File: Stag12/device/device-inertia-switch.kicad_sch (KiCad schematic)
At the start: 2 parts

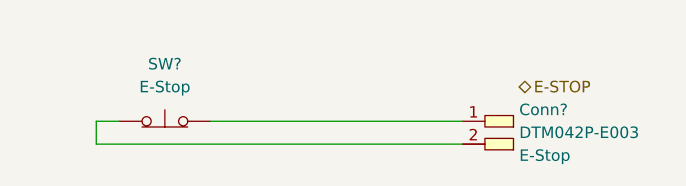
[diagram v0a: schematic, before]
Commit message: Changed filepaths
Makes graphical explorers a bit neater

TODO: Decide on new paths for each device (maybe geographical?)
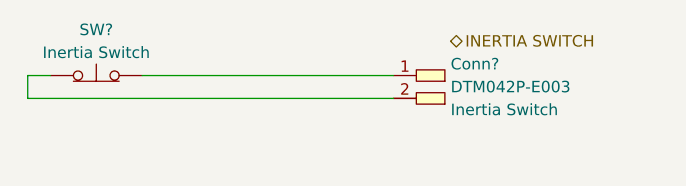
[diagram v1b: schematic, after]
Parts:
- removed Conn?: Deutsch_DTM_2P_Pin, symbol Connectors_SUFST:Deutsch_DTM_2P_Pin
- removed SW?: E-Stop, symbol Switch:SW_Push_Open
- added Conn?: Deutsch_DTM_2P_Pin, symbol Connectors_SUFST:Deutsch_DTM_2P_Pin
- added SW?: Inertia Switch, symbol Switch:SW_Push_Open
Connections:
- new net: Conn?.2, SW?.1 (A)
- new net: Conn?.1, SW?.2 (B)
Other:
- title: DEVICE - E-STOP -> DEVICE - INERTIA SWITCH
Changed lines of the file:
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@@
 	(paper "A4")
 	(title_block
-		(title "DEVICE - E-STOP")
-	)
-	(wire
-		(pts
-			(xy 119.38 99.06) (xy 116.84 99.06)
-		)
-		(stroke
-			(width 0)
-			(type default)
-		)
-	)
-	(wire
-		(pts
-			(xy 116.84 101.6) (xy 157.48 101.6)
-		)
-		(stroke
-			(width 0)
-			(type default)
-		)
-	)
-	(wire
-		(pts
-			(xy 116.84 99.06) (xy 116.84 101.6)
-		)
-		(stroke
-			(width 0)
-			(type default)
-		)
-	)
-	(wire
-		(pts
-			(xy 129.54 99.06) (xy 157.48 99.06)
-		)
-		(stroke
-			(width 0)
-			(type default)
-		)
-	)
-	(hierarchical_label "E-STOP"
+		(title "DEVICE - INERTIA SWITCH")
+	)
+	(wire
+		(pts
+			(xy 109.22 96.52) (xy 149.86 96.52)
+		)
+		(stroke
+			(width 0)
+			(type default)
+		)
+	)
+	(wire
+		(pts
+			(xy 121.92 93.98) (xy 149.86 93.98)
+		)
+		(stroke
+			(width 0)
+			(type default)
+		)
+	)
+	(wire
+		(pts
+			(xy 109.22 93.98) (xy 109.22 96.52)
+		)
+		(stroke
+			(width 0)
+			(type default)
+		)
+	)
+	(wire
+		(pts
+			(xy 111.76 93.98) (xy 109.22 93.98)
+		)
+		(stroke
+			(width 0)
+			(type default)
+		)
+	)
+	(hierarchical_label "INERTIA SWITCH"
 		(shape bidirectional)
-		(at 163.83 95.25 0)
+		(at 156.21 90.17 0)
 		(effects
 			(font
@@
 	(symbol
 		(lib_id "Switch:SW_Push_Open")
-		(at 124.46 99.06 0)
+		(at 116.84 93.98 0)
 		(unit 1)
 		(exclude_from_sim no)
@@
 		(fields_autoplaced yes)
 		(property "Reference" "SW?"
-			(at 124.46 92.71 0)
-			(effects
-				(font
-					(size 1.27 1.27)
-				)
-			)
-		)
-		(property "Value" "E-Stop"
-			(at 124.46 95.25 0)
+			(at 116.84 88.9 0)
+			(effects
+				(font
+					(size 1.27 1.27)
+				)
+			)
+		)
+		(property "Value" "Inertia Switch"
+			(at 116.84 91.44 0)
 			(effects
 				(font
@@
 		)
 		(property "Footprint" ""
-			(at 124.46 93.98 0)
+			(at 116.84 88.9 0)
 			(effects
 				(font
@@
 		)
 		(property "Datasheet" "~"
-			(at 124.46 93.98 0)
+			(at 116.84 88.9 0)
 			(effects
 				(font
@@
 		)
 		(property "Description" ""
-			(at 124.46 99.06 0)
+			(at 116.84 93.98 0)
 			(effects
 				(font
@@
 		)
 		(property "Conn Name" ""
-			(at 124.46 95.25 0)
+			(at 116.84 90.17 0)
 			(effects
 				(font
@@
 		)
 		(instances
-			(project "Stag11"
-				(path "/03011643-0690-4b85-ab78-d6a62dae52b1/3cdef822-b27b-4a71-b67b-74c9f7188311"
+			(project "Stag12"
+				(path "/03011643-0690-4b85-ab78-d6a62dae52b1/f29d1e22-db5a-4e21-943f-a4075fd10598"
 					(reference "SW?")
 					(unit 1)
 				)
-				(path "/03011643-0690-4b85-ab78-d6a62dae52b1/8cb55a6b-0d65-49e2-b083-4cc99e15786c"
-					(reference "SW?")
-					(unit 1)
-				)
-				(path "/03011643-0690-4b85-ab78-d6a62dae52b1/a345ed85-d8da-42e0-9850-81cfb8a2389f"
-					(reference "SW?")
-					(unit 1)
-				)
 			)
 		)
@@
 	(symbol
 		(lib_id "Connectors_SUFST:Deutsch_DTM_2P_Pin")
-		(at 159.385 106.045 180)
+		(at 151.765 100.965 180)
 		(unit 1)
 		(exclude_from_sim no)
@@
 		(fields_autoplaced yes)
 		(property "Reference" "Conn?"
-			(at 163.83 97.79 0)
+			(at 156.21 92.71 0)
 			(effects
 				(font
@@
 		)
 		(property "Value" "Deutsch_DTM_2P_Pin"
-			(at 159.385 106.045 0)
+			(at 151.765 100.965 0)
 			(effects
 				(font
@@
 		)
 		(property "Footprint" ""
-			(at 159.385 104.14 0)
+			(at 151.765 99.06 0)
 			(effects
 				(font
@@
 		)
 		(property "Datasheet" ""
-			(at 159.385 104.14 0)
+			(at 151.765 99.06 0)
 			(effects
 				(font
@@
 		)
 		(property "Description" ""
-			(at 159.385 106.045 0)
+			(at 151.765 100.965 0)
 			(effects
 				(font
@@
 		)
 		(property "P/N" "DTM042P-E003"
-			(at 163.83 100.33 0)
+			(at 156.21 95.25 0)
 			(effects
 				(font
@@
 			)
 		)
-		(property "Conn Name" "E-Stop"
-			(at 163.83 102.87 0)
+		(property "Conn Name" "Inertia Switch"
+			(at 156.21 97.79 0)
 			(effects
 				(font
@@
 		)
 		(instances
-			(project "Stag11"
-				(path "/03011643-0690-4b85-ab78-d6a62dae52b1/3cdef822-b27b-4a71-b67b-74c9f7188311"
+			(project "Stag12"
+				(path "/03011643-0690-4b85-ab78-d6a62dae52b1/f29d1e22-db5a-4e21-943f-a4075fd10598"
 					(reference "Conn?")
 					(unit 1)
-				)
-				(path "/03011643-0690-4b85-ab78-d6a62dae52b1/8cb55a6b-0d65-49e2-b083-4cc99e15786c"
-					(reference "Conn?")
-					(unit 1)
-				)
-				(path "/03011643-0690-4b85-ab78-d6a62dae52b1/a345ed85-d8da-42e0-9850-81cfb8a2389f"
-					(reference "Conn?")
-					(unit 1)

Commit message: More progress on front loom
autosport my beloved
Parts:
- gave numbers to parts that had none: 2
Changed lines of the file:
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@@
 		(dnp no)
 		(fields_autoplaced yes)
-		(property "Reference" "SW?"
+		(property "Reference" "SW13"
 			(at 116.84 88.9 0)
 			(effects
@@
 		(instances
 			(project "Stag12"
-				(path "/03011643-0690-4b85-ab78-d6a62dae52b1/f29d1e22-db5a-4e21-943f-a4075fd10598"
-					(reference "SW?")
+				(path "/03011643-0690-4b85-ab78-d6a62dae52b1/6406ca02-a7b3-44d1-a9c8-8d41c28475a6"
+					(reference "SW13")
 					(unit 1)
 				)
@@
 		(dnp no)
 		(fields_autoplaced yes)
-		(property "Reference" "Conn?"
+		(property "Reference" "Conn41"
 			(at 156.21 92.71 0)
 			(effects
@@
 		(instances
 			(project "Stag12"
-				(path "/03011643-0690-4b85-ab78-d6a62dae52b1/f29d1e22-db5a-4e21-943f-a4075fd10598"
-					(reference "Conn?")
+				(path "/03011643-0690-4b85-ab78-d6a62dae52b1/6406ca02-a7b3-44d1-a9c8-8d41c28475a6"
+					(reference "Conn41")
 					(unit 1)
 				)
